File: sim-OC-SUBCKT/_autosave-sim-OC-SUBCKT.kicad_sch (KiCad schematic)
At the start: 14 parts, among them Q1 PMOS, Q2 PMOS

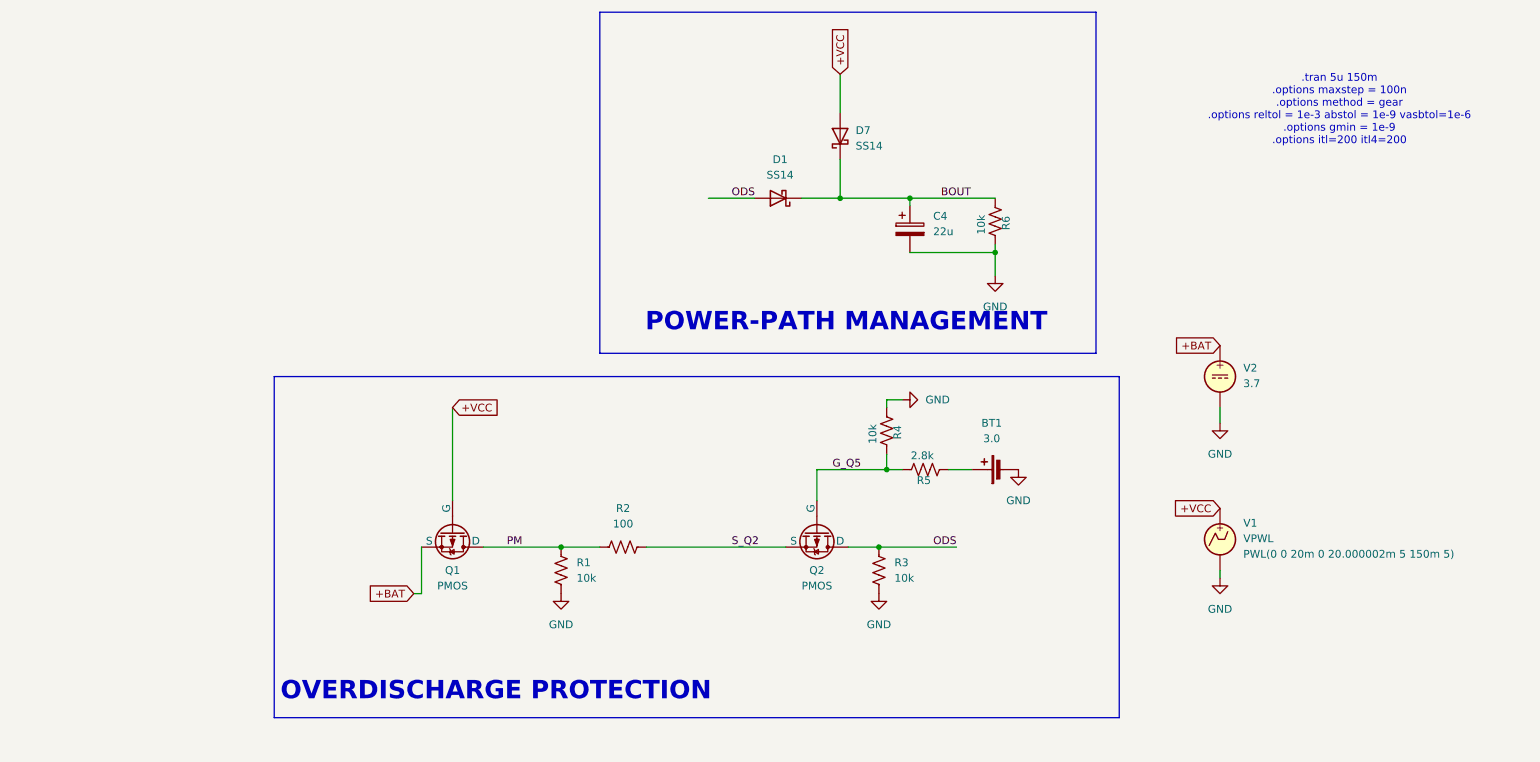
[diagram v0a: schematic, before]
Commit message: simulations fixed with solid model files, results documented
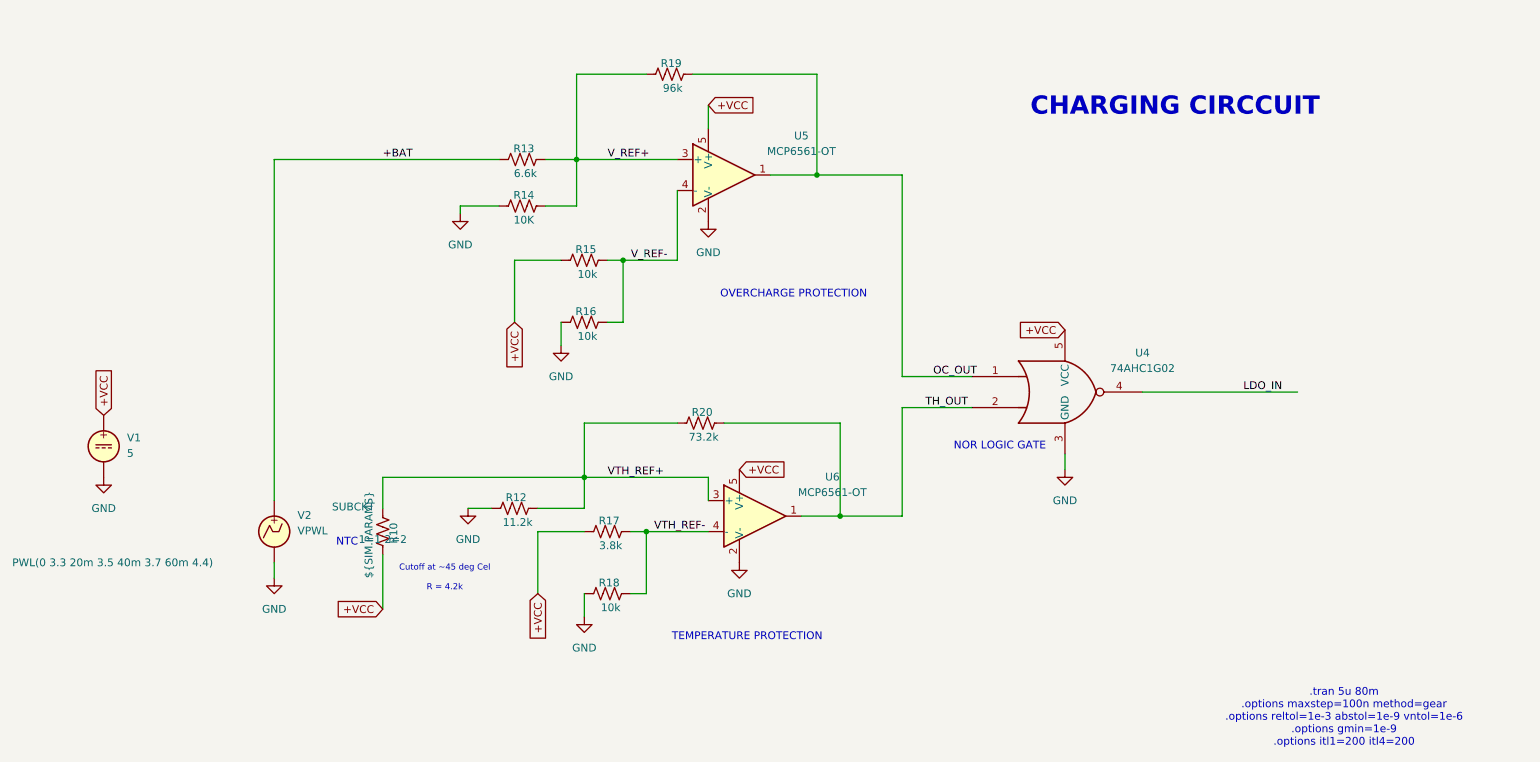
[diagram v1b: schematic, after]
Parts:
- removed BT1: 3.0, symbol Device:Battery_Cell
- removed C4: 22u, symbol Device:C_Polarized
- removed D1, D7: SS14, Diode_SMD:D_SMA, symbol Diode:SS14
- removed Q1, Q2: PMOS, symbol Simulation_SPICE:PMOS
- removed R1, R3, R4, R6: 10k, symbol Device:R_US
- removed R2: 100, symbol Device:R_US
- removed R5: 2.8k, symbol Device:R_US
- removed V1: VPWL, symbol Simulation_SPICE:VPWL
- removed V2: 3.7, symbol Simulation_SPICE:VDC
- added R10: ${SIM.PARAMS}, symbol Device:R_US
- added R12: 11.2k, symbol Device:R_US
- added R13: 6.6k, symbol Device:R_US
- added R14: 10K, symbol Device:R_US
- added R15, R16, R18: 10k, symbol Device:R_US
- added R17: 3.8k, symbol Device:R_US
- added R19: 96k, symbol Device:R_US
- added R20: 73.2k, symbol Device:R_US
- added U4: 74AHC1G02, symbol 74xGxx:74AHC1G02
- added U5, U6: MCP6561-OT, Package_TO_SOT_SMD:SOT-23-5, symbol Comparator:MCP6561-OT
- added V1: 5, symbol Simulation_SPICE:VDC
- added V2: VPWL, symbol Simulation_SPICE:VPWL
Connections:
- net +BAT: now also R13.1, V2.1
- net +VCC: now also R10.2, R15.1, R17.1, U4.5 (VCC), U5.5 (V+), U6.5 (V+), V1.1
- net GND: now also R12.1, R14.1, R16.1, R18.1, U4.3 (GND), U5.2 (V-), U6.2 (V-), V1.2, V2.2
- new net LDO_IN: U4.4
- new net OC_OUT: R19.2, U4.1, U5.1
- new net TH_OUT: R20.2, U4.2, U6.1
- new net VTH_REF+: R10.1, R12.2, R20.1, U6.3 (+)
- new net VTH_REF-: R17.2, R18.2, U6.4 (-)
- new net V_REF+: R13.2, R14.2, R19.1, U5.3 (+)
- new net V_REF-: R15.2, R16.2, U5.4 (-)
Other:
- note added: ".tran 5u 80m .options maxstep=100n method=gear .options reltol=1e-3 abstol=1e-9 vntol=1e-6 .options gmin=1e-9 .options itl1=200 itl4=200"
- note added: "CHARGING CIRCCUIT"
- note added: "Cutoff at ~45 deg Cel R = 4.2k"
- note added: "NOR LOGIC GATE"
- note added: "NTC"
- note added: "OVERCHARGE PROTECTION"
- note added: "TEMPERATURE PROTECTION"
- note removed: ".tran 5u 150m .options maxstep = 100n .options method = gear .options reltol = 1e-3 abstol = 1e-9 vasbtol=1e-6 .options gmin = 1e-9 .options itl=200 itl4=200"
- note removed: "OVERDISCHARGE PROTECTION"
- note removed: "POWER-PATH MANAGEMENT"
